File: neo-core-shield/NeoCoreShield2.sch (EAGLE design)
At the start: 45 parts, among them J6 BINDER_M12_PAR_8_DIP, J7 BINDER_M12_PAR_8_DIP, J8 BINDER_M12_PAR_8_DIP, J9 BINDER_M12_PAR_8_DIP, Q1 2.5A/30V/105mΩ, Q2 310mA/60V/1.6Ω, Q3 2.5A/30V/105mΩ, Q4 2.5A/30V/105mΩ, Q5 310mA/60V/1.6Ω, Q6 310mA/60V/1.6Ω

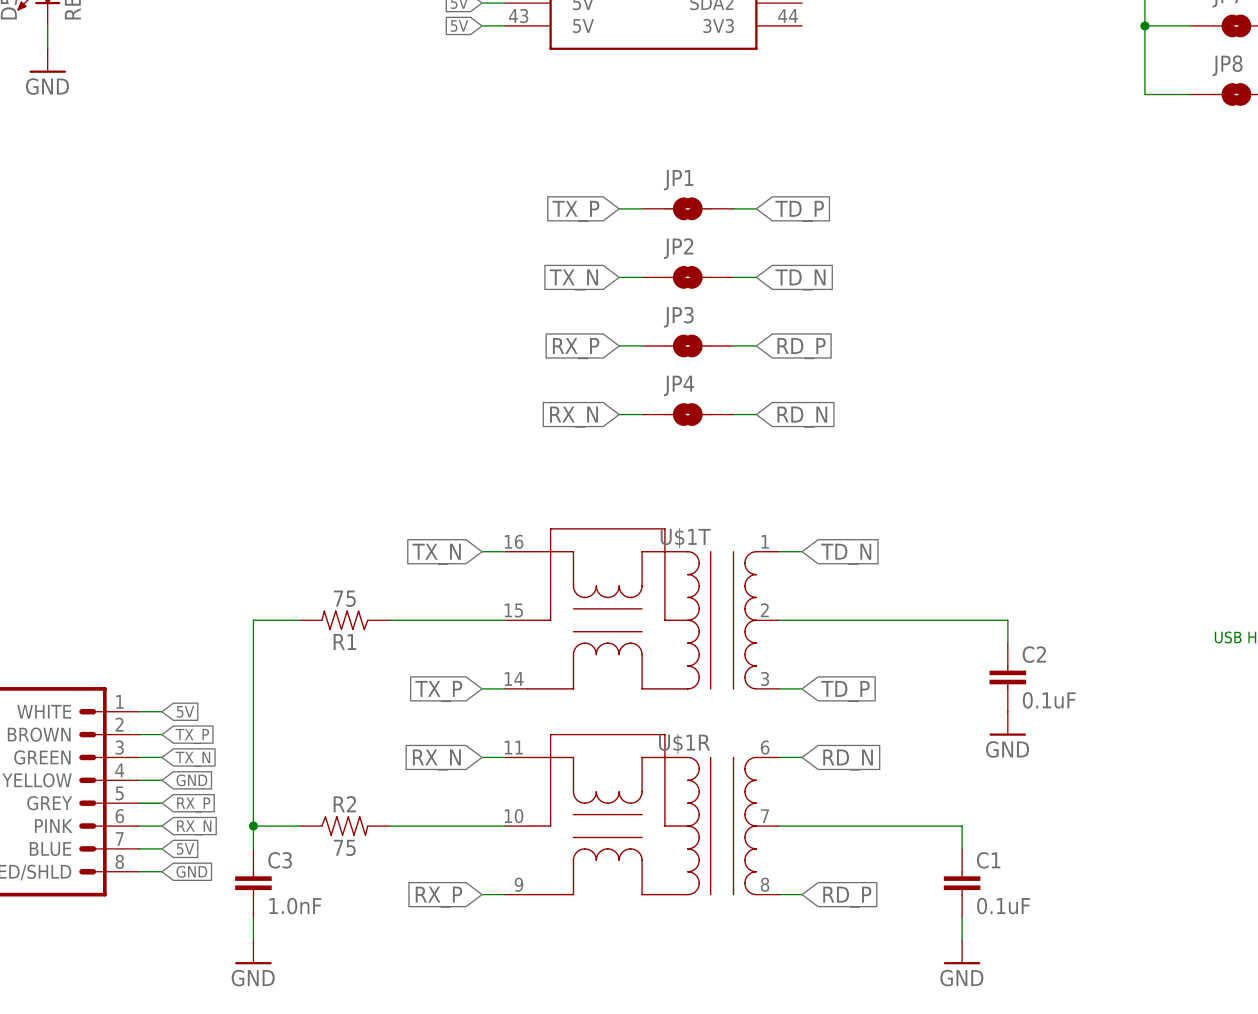
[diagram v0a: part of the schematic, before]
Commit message: Rectangular layout for holes
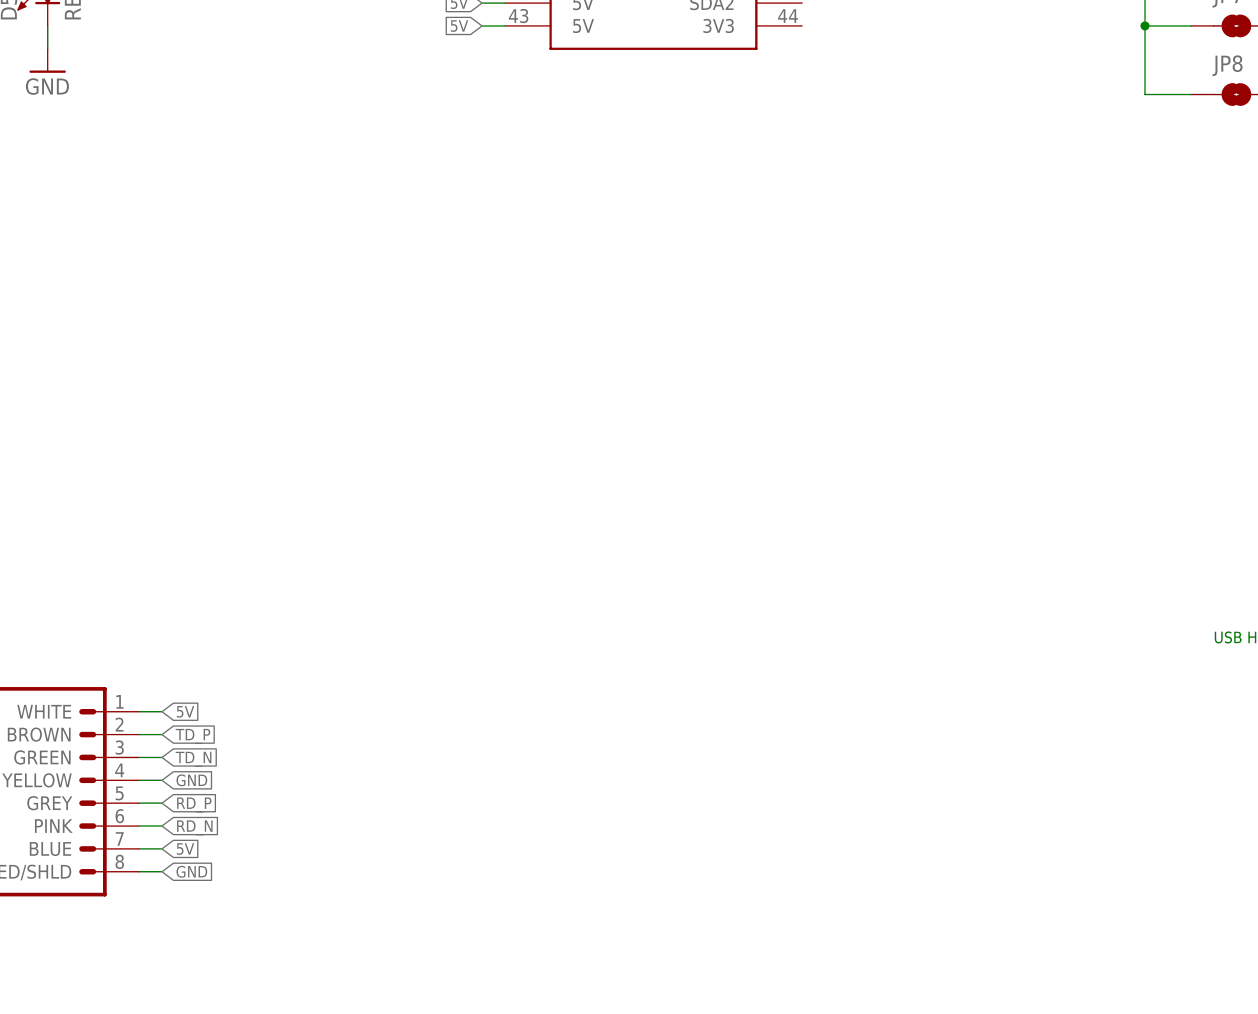
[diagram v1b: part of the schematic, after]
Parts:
- removed C1, C2: 0.1uF, SparkFun-Capacitors:0.1UF-0603-25V-(+80/-20%)
- removed C3: 1.0nF, SparkFun-Capacitors:1.0UF-1206-50V-10%
- removed JP1, JP2, JP3, JP4: JUMPER-SMT_2_NO_SILK, SparkFun-Jumpers:JUMPER-SMT_2_NO_SILK
- removed R1, R2: 75, SparkFun-Resistors:75KOHM-0603-1/10W-1%
- removed U$1: ETH-TRANS, ethernet transformer:ETH-TRANS
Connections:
- removed net ETH_TD0_GND: C1.1, U$1R.CT
- removed net ETH_TD1_GND: C2.1, U$1T.CT
- removed net ETH_TERM_MID: C3.1, R1.2, R2.1
- removed net N$11: R1.1, U$1T.XCT
- removed net N$3: R2.2, U$1R.XCT
- removed net RX_N: J9.PINK, JP4.1, U$1R.X+
- removed net RX_P: J9.GREY, JP3.1, U$1R.X-
- removed net TX_N: J9.GREEN, JP2.1, U$1T.X+
- removed net TX_P: J9.BROWN, JP1.1, U$1T.X-
- net GND: no longer C1.2, C2.2, C3.2
- net RD_N: now also J9.PINK; no longer JP4.2, U$1R.D+
- net RD_P: now also J9.GREY; no longer JP3.2, U$1R.D-
- net TD_N: now also J9.GREEN; no longer JP2.2, U$1T.D+
- net TD_P: now also J9.BROWN; no longer JP1.2, U$1T.D-
